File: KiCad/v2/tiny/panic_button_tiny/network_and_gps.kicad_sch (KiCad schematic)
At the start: 2 parts, among them J2 JAE_SIM_Card_SF72S006, U5 SIM7670G-LNGV

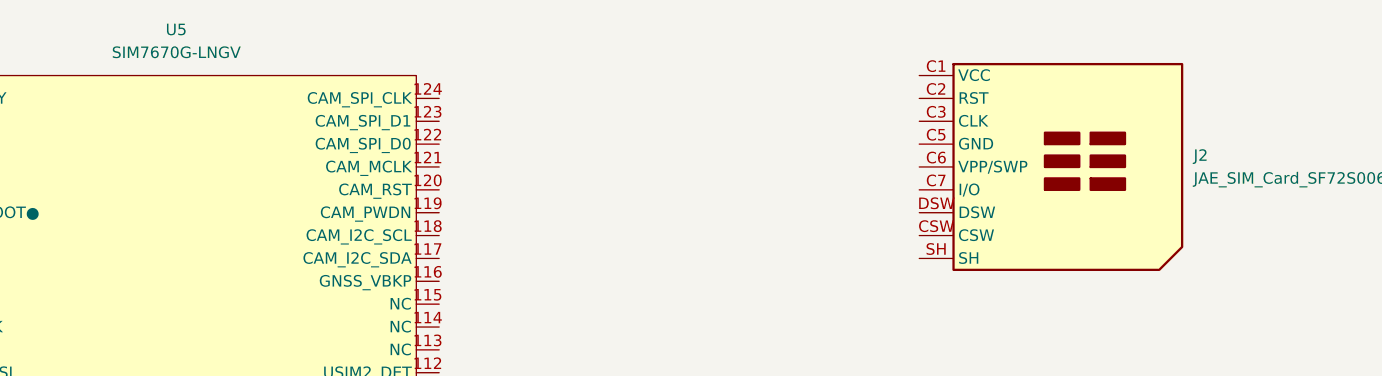
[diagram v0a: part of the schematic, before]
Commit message: [UPDATE] the structure of the KiCad design for the tiny version
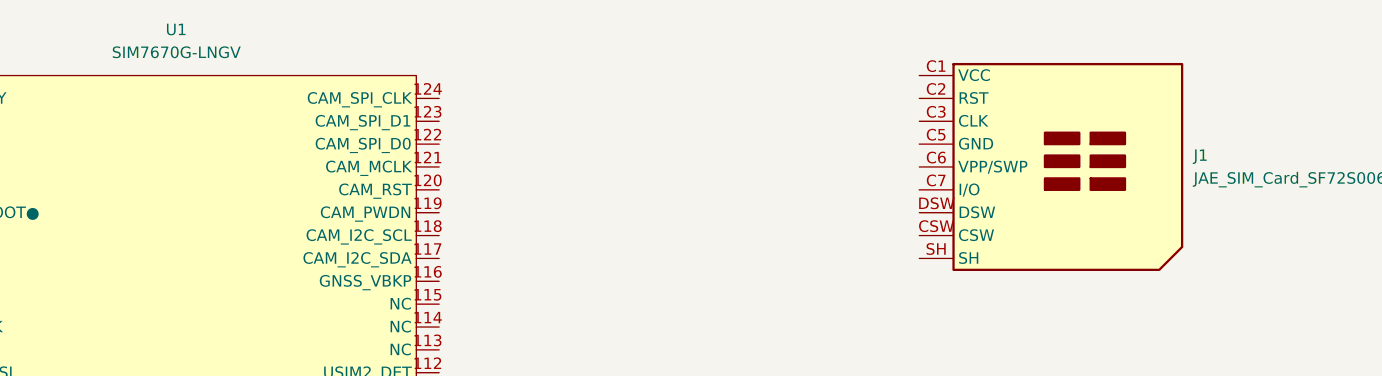
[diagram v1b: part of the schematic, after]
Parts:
- renumbered J2 to J1, U5 to U1
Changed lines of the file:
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@@
 		(dnp no)
 		(fields_autoplaced yes)
-		(property "Reference" "J2"
+		(property "Reference" "J1"
 			(at 248.92 30.4799 0)
 			(show_name no)
@@
 			(project "panic_button_tiny"
 				(path "/c4eb92e9-b42f-4db0-b1d9-0ef70f7ca601/264a0769-bcc3-4bdf-b2a9-76b0d2a047ac"
-					(reference "J2")
+					(reference "J1")
 					(unit 1)
 				)
@@
 		(dnp no)
 		(fields_autoplaced yes)
-		(property "Reference" "U5"
+		(property "Reference" "U1"
 			(at 135.89 16.51 0)
 			(show_name no)
@@
 			(project "panic_button_tiny"
 				(path "/c4eb92e9-b42f-4db0-b1d9-0ef70f7ca601/264a0769-bcc3-4bdf-b2a9-76b0d2a047ac"
-					(reference "U5")
+					(reference "U1")
 					(unit 1)
 				)

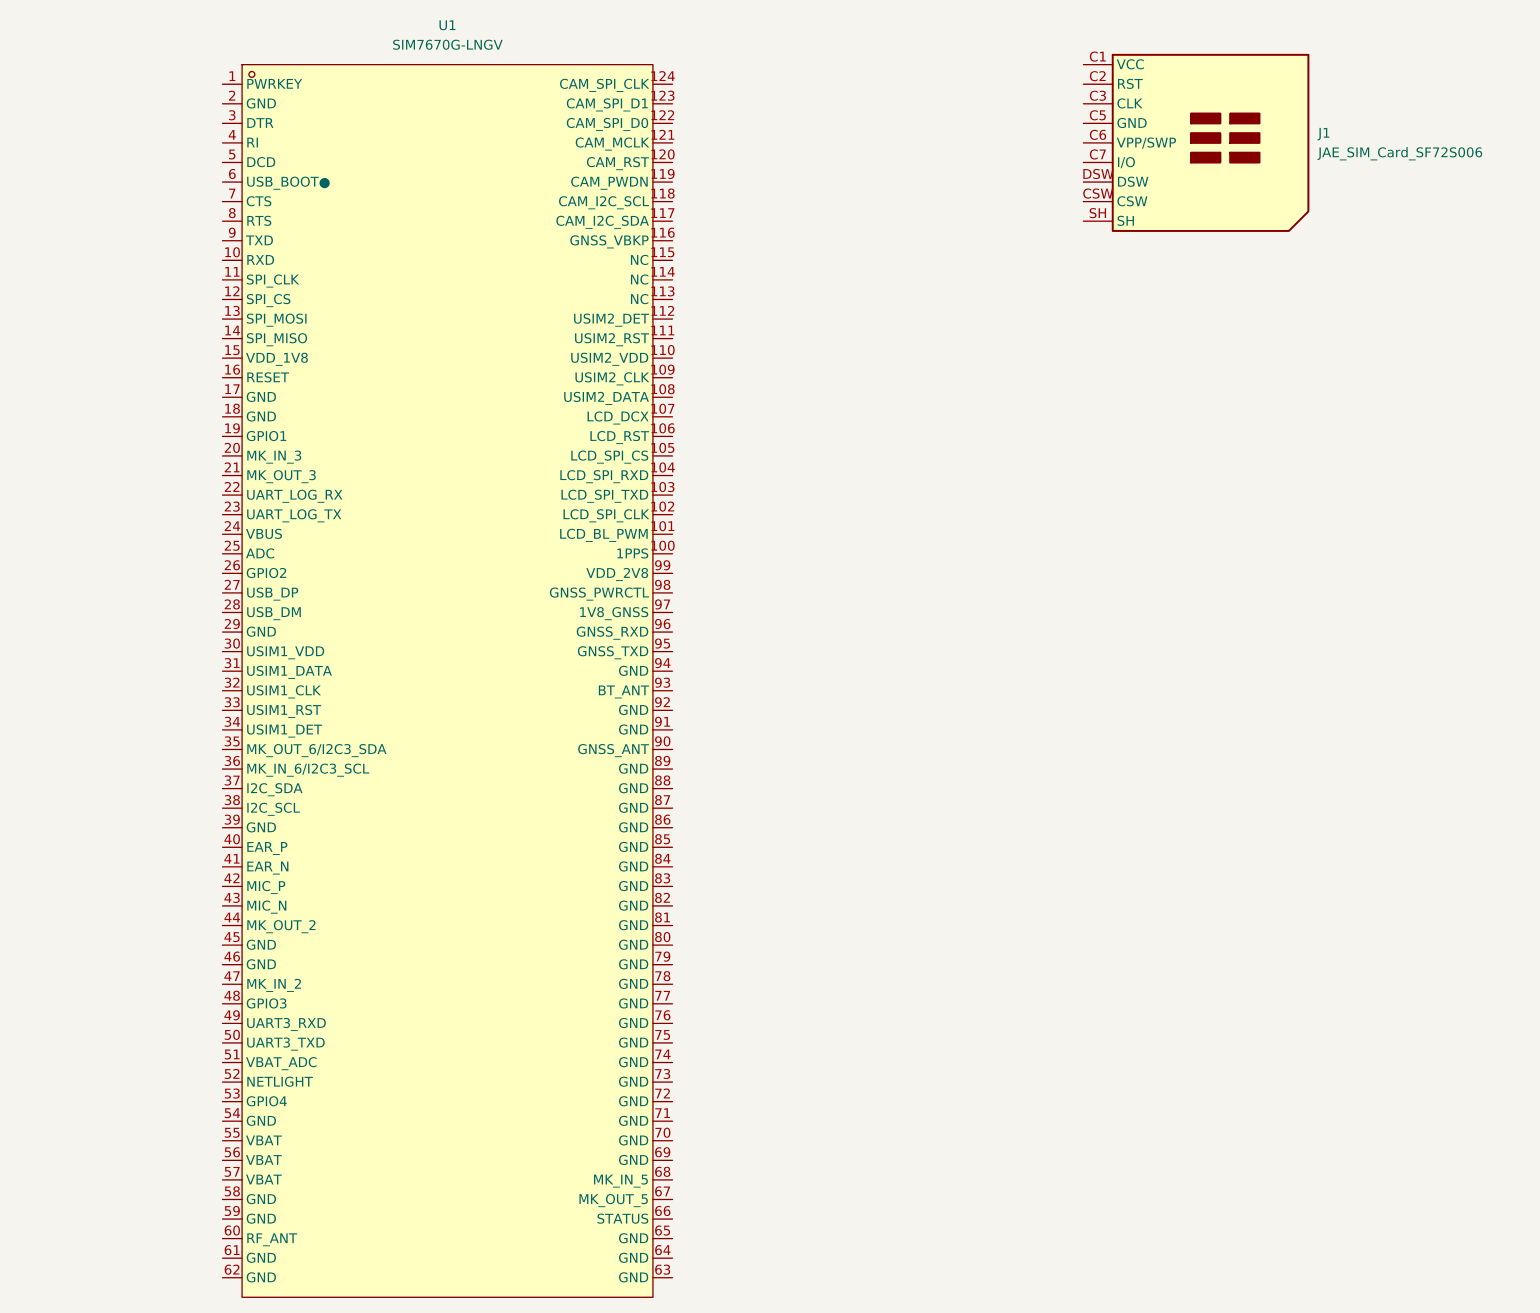
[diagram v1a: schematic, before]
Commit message: [ADD] GND symbols to obvious locations requirering it
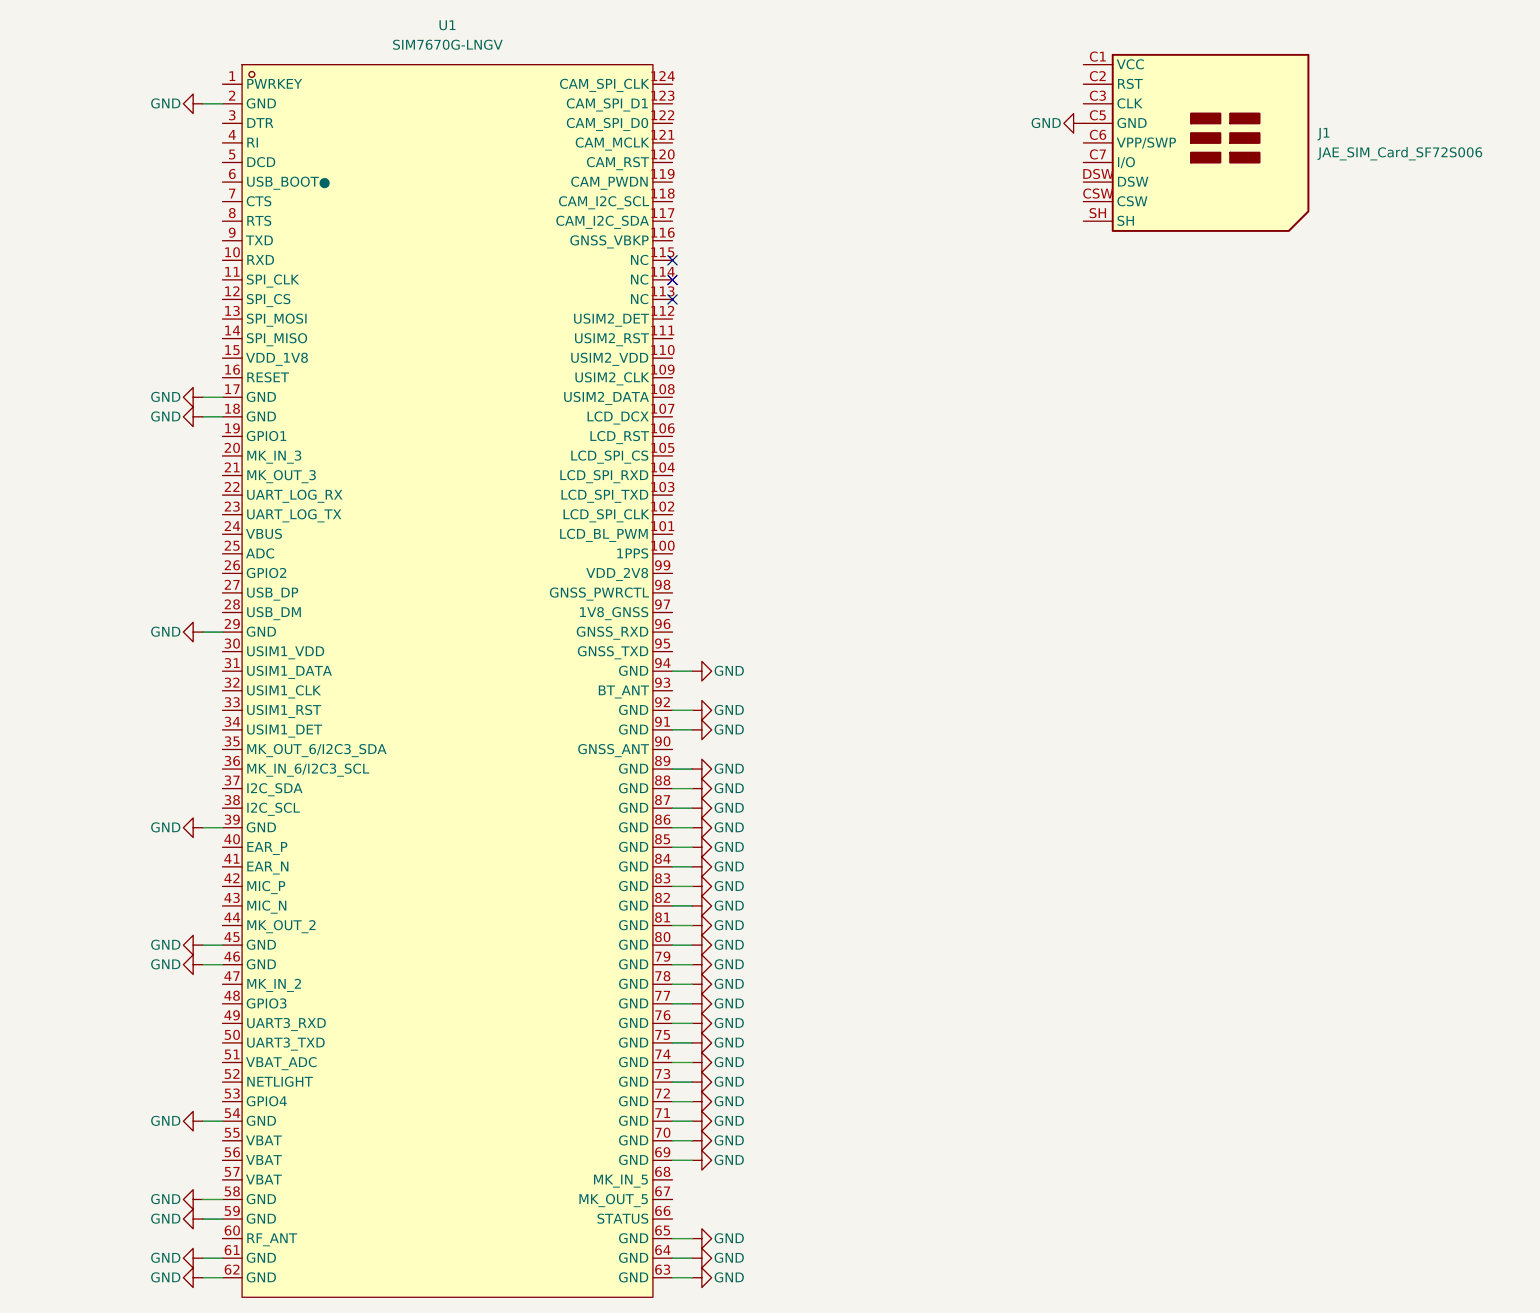
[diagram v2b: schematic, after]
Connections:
- net GND: now reaches J1.C5 (GND)
- net GND: now also U1.17 (GND), U1.18 (GND), U1.2 (GND), U1.29 (GND), U1.39 (GND), U1.45 (GND), U1.46 (GND), U1.54 (GND), U1.58 (GND), U1.59 (GND), U1.61 (GND), U1.62 (GND), U1.63 (GND), U1.64 (GND), U1.65 (GND), U1.69 (GND), U1.70 (GND), U1.71 (GND), U1.72 (GND), U1.73 (GND), U1.74 (GND), U1.75 (GND), U1.76 (GND), U1.77 (GND), U1.78 (GND), U1.79 (GND), U1.80 (GND), U1.81 (GND), U1.82 (GND), U1.83 (GND), U1.84 (GND), U1.85 (GND), U1.86 (GND), U1.87 (GND), U1.88 (GND), U1.89 (GND), U1.91 (GND), U1.92 (GND), U1.94 (GND)
- no-connect marks 0 -> 3

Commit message: [UPDATE] the schematic with a buzzer and wirering for the different components
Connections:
- net power_on_pulse: now reaches U1.1 (PWRKEY)
- net UART RXD: now reaches U1.10 (RXD)
- net battery_voltage_sense: now reaches U1.51 (VBAT_ADC)
- net modem_status: now reaches U1.66 (STATUS)
- net UART TXD: now reaches U1.9 (TXD)
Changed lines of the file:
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@@
+		)
+	)
+	(hierarchical_label "battery_voltage_sense"
+		(shape input)
+		(at 106.68 151.13 180)
+		(effects
+			(font
+				(size 1.27 1.27)
+			)
+			(justify right)
+		)
+	)
+	(hierarchical_label "UART RXD"
+		(shape input)
+		(at 106.68 46.99 180)
+		(effects
+			(font
+				(size 1.27 1.27)
+			)
+			(justify right)
+		)
+	)
+	(hierarchical_label "power_on_pulse"
+		(shape input)
+		(at 106.68 24.13 180)
+		(effects
+			(font
+				(size 1.27 1.27)
+			)
+			(justify right)
+		)
+	)
+	(hierarchical_label "UART TXD"
+		(shape input)
+		(at 106.68 44.45 180)
+		(effects
+			(font
+				(size 1.27 1.27)
+			)
+			(justify right)
+		)
+	)
+	(hierarchical_label "modem_status"
+		(shape input)
+		(at 165.1 171.45 0)
+		(effects
+			(font
+				(size 1.27 1.27)
+			)
+			(justify left)
 		)
 	)

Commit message: [UPDATE] some connections in the schematic
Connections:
- net UART RXD renamed UART (RXD)
- net UART TXD renamed UART (TXD)
- net power_on_pulse renamed power-on_pulse
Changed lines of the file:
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@@
 		)
 	)
-	(hierarchical_label "UART RXD"
+	(hierarchical_label "UART (RXD)"
 		(shape input)
 		(at 106.68 46.99 180)
@@
 		)
 	)
-	(hierarchical_label "power_on_pulse"
+	(hierarchical_label "power-on_pulse"
 		(shape input)
 		(at 106.68 24.13 180)
@@
 		)
 	)
-	(hierarchical_label "UART TXD"
+	(hierarchical_label "UART (TXD)"
 		(shape input)
 		(at 106.68 44.45 180)
